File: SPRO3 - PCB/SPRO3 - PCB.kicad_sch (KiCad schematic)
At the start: 14 parts

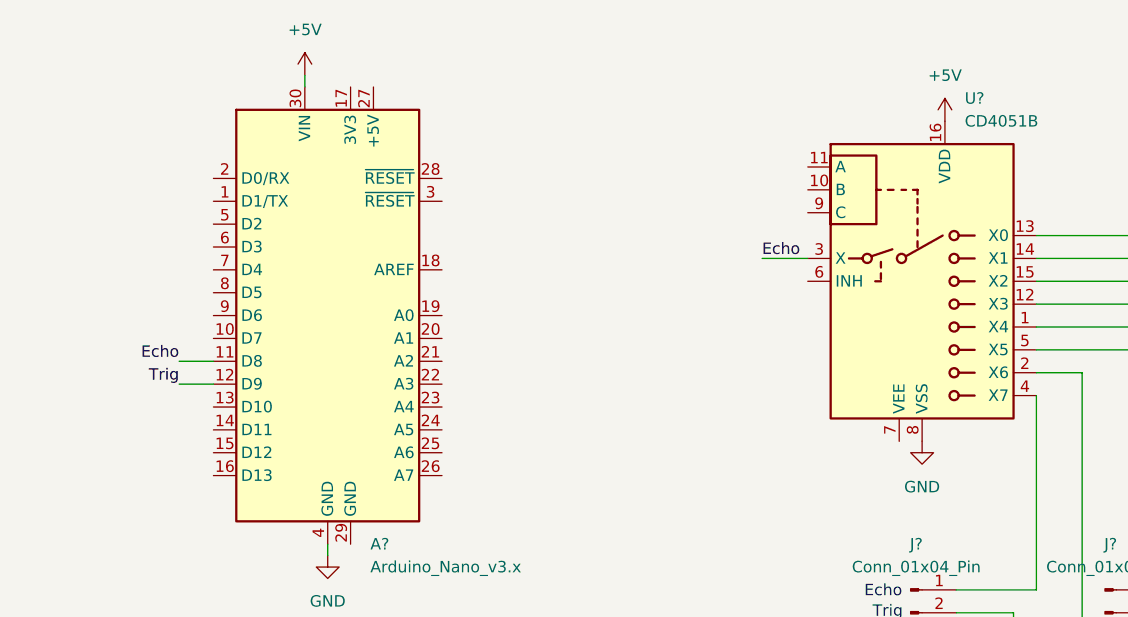
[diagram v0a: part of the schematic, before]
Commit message: Added bypass capacitor to MUX
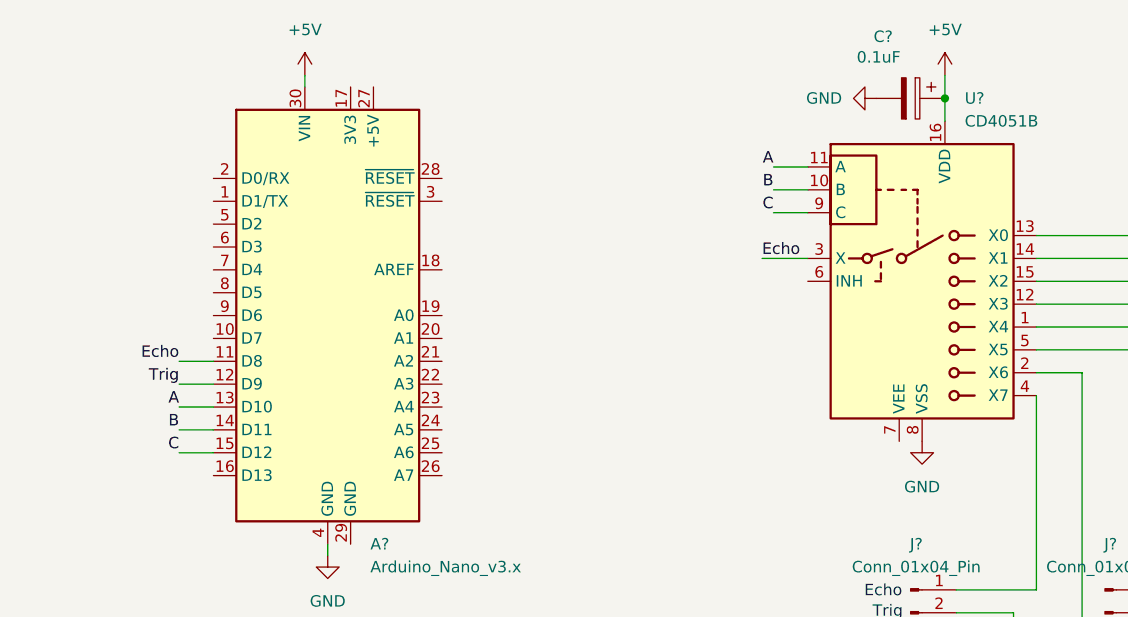
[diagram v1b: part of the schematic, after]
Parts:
- added C?: 0.1uF, symbol Device:C_Polarized
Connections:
- net +5V: now also C?.1
- net GND: now also C?.2
- net A: now reaches A?.13 (D10)
- net A: now also U?.11 (A)
- net B: now reaches A?.14 (D11)
- net B: now also U?.10 (B)
- net C: now reaches A?.15 (D12)
- net C: now also U?.9 (C)

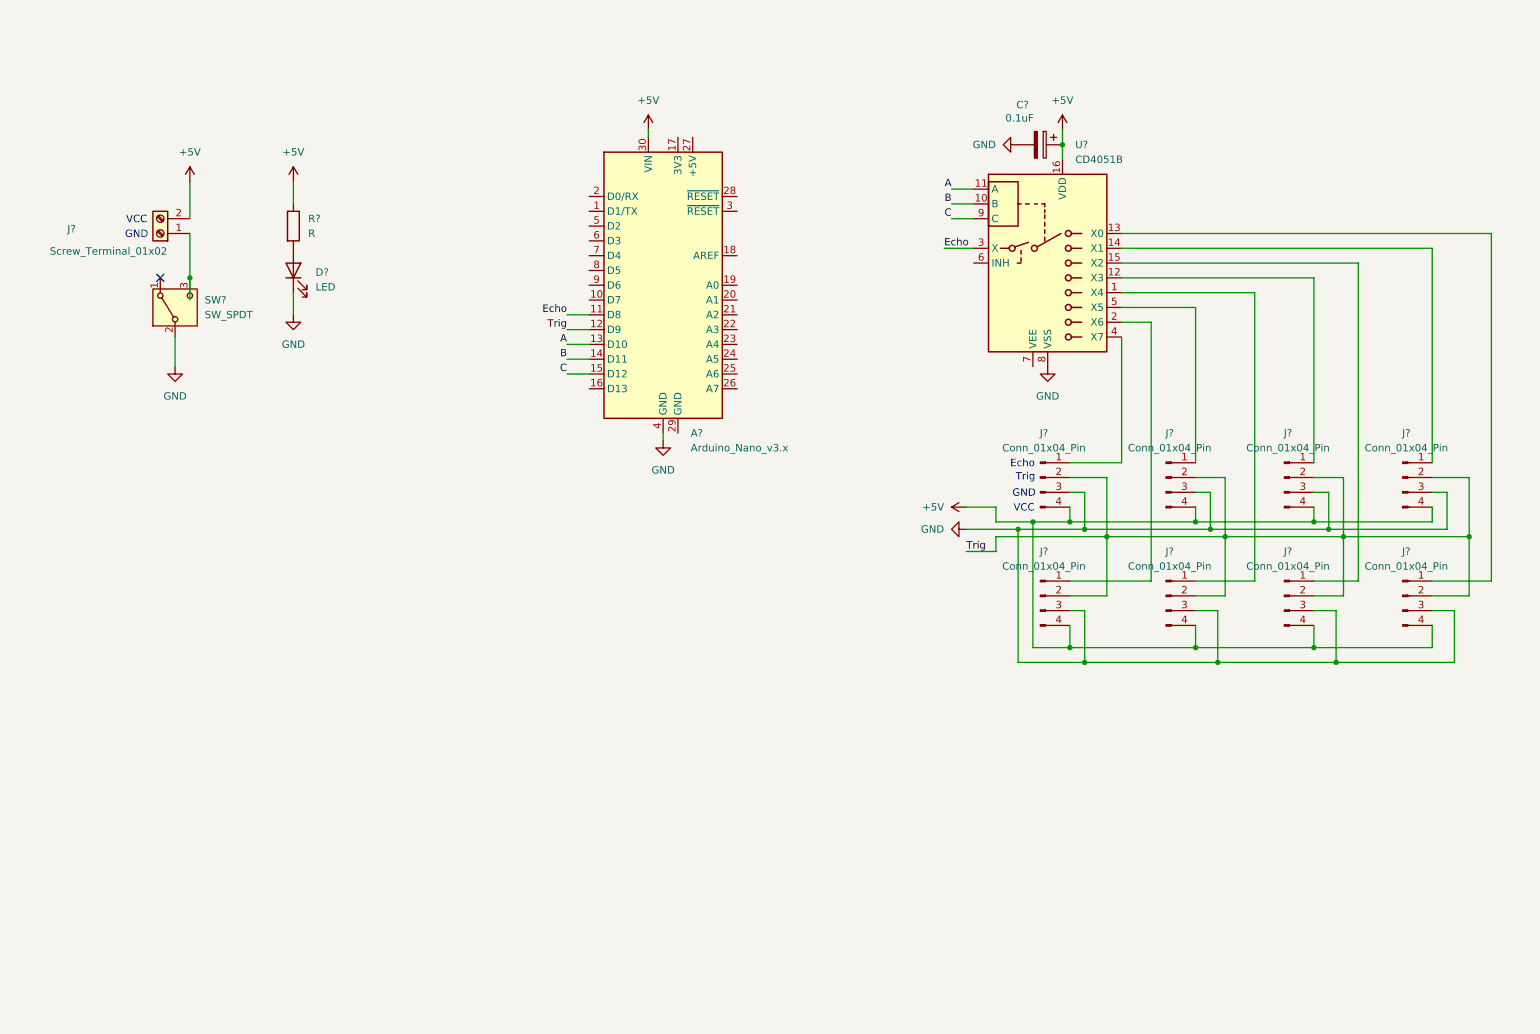
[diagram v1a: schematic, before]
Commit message: udated MUX schematic
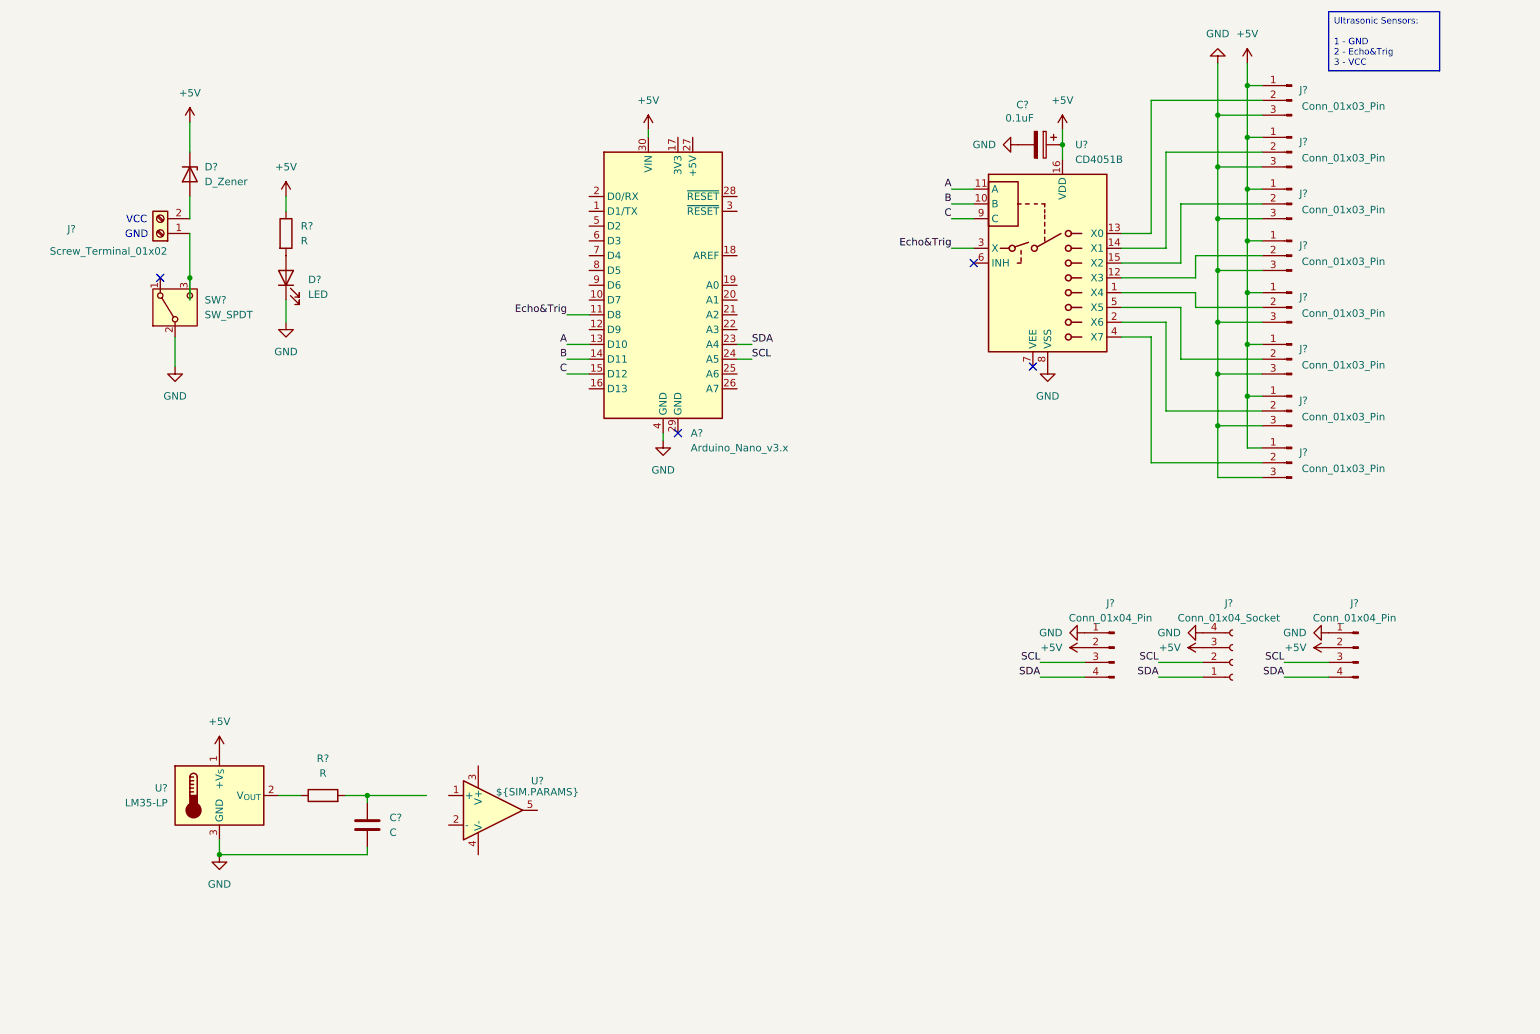
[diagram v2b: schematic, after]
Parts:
- removed J? (x8): Conn_01x04_Pin, symbol Connector:Conn_01x04_Pin
- added C?: C, symbol Device:C
- added D?: D_Zener, symbol Device:D_Zener
- added J? (x8): Conn_01x03_Pin, symbol Connector:Conn_01x03_Pin
- added J?: Conn_01x04_Socket, symbol Connector:Conn_01x04_Socket
- added J? (x2): Conn_01x04_Pin, symbol Connector:Conn_01x04_Pin
- added R?: R, symbol Device:R
- added U?: ${SIM.PARAMS}, symbol Simulation_SPICE:OPAMP
- added U?: LM35-LP, Package_TO_SOT_THT:TO-92_Inline, symbol Sensor_Temperature:LM35-LP
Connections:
- net +5V: now also D?.1 (K), J?.1 (Pin_1), J?.1 (Pin_1), J?.1 (Pin_1), J?.1 (Pin_1), J?.1 (Pin_1), J?.1 (Pin_1), J?.1 (Pin_1), J?.1 (Pin_1), J?.2 (Pin_2), J?.2 (Pin_2), J?.3 (Pin_3), U?.1 (+V_{S}); no longer J?.2 (Pin_2)
- net GND: now also C?.2, J?.1 (Pin_1), J?.1 (Pin_1), J?.3 (Pin_3), J?.3 (Pin_3), J?.3 (Pin_3), J?.3 (Pin_3), J?.3 (Pin_3), J?.3 (Pin_3), J?.3 (Pin_3), J?.3 (Pin_3), J?.4 (Pin_4), U?.3 (GND)
- net SDA: now reaches A?.23 (A4)
- net SDA: now also J?.1 (Pin_1), J?.4 (Pin_4), J?.4 (Pin_4)
- net SCL: now reaches A?.24 (A5)
- net SCL: now also J?.2 (Pin_2), J?.3 (Pin_3), J?.3 (Pin_3)
- net at U?.15 (X2): now also J?.2 (Pin_2)
- net at U?.4 (X7): now also J?.2 (Pin_2)
- net at U?.2 (X6): now also J?.2 (Pin_2)
- net at U?.13 (X0): now also J?.2 (Pin_2)
- net at U?.1 (X4): now also J?.2 (Pin_2)
- net at U?.12 (X3): now also J?.2 (Pin_2)
- net at U?.14 (X1): now also J?.2 (Pin_2)
- net at U?.5 (X5): now also J?.2 (Pin_2)
- net Echo renamed Echo&Trig
- net Trig: no longer names the net of A?.12 (D9)
- new net: R?.1, U?.2 (V_{OUT})
- new net: C?.1, R?.2
- new net: D?.2 (A), J?.2 (Pin_2)
- no-connect marks 1 -> 4
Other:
- note removed: "Echo"
- note removed: "Trig"
- moved on the sheet: D?, R?

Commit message: Added Kicad files for the second PCB that we are making
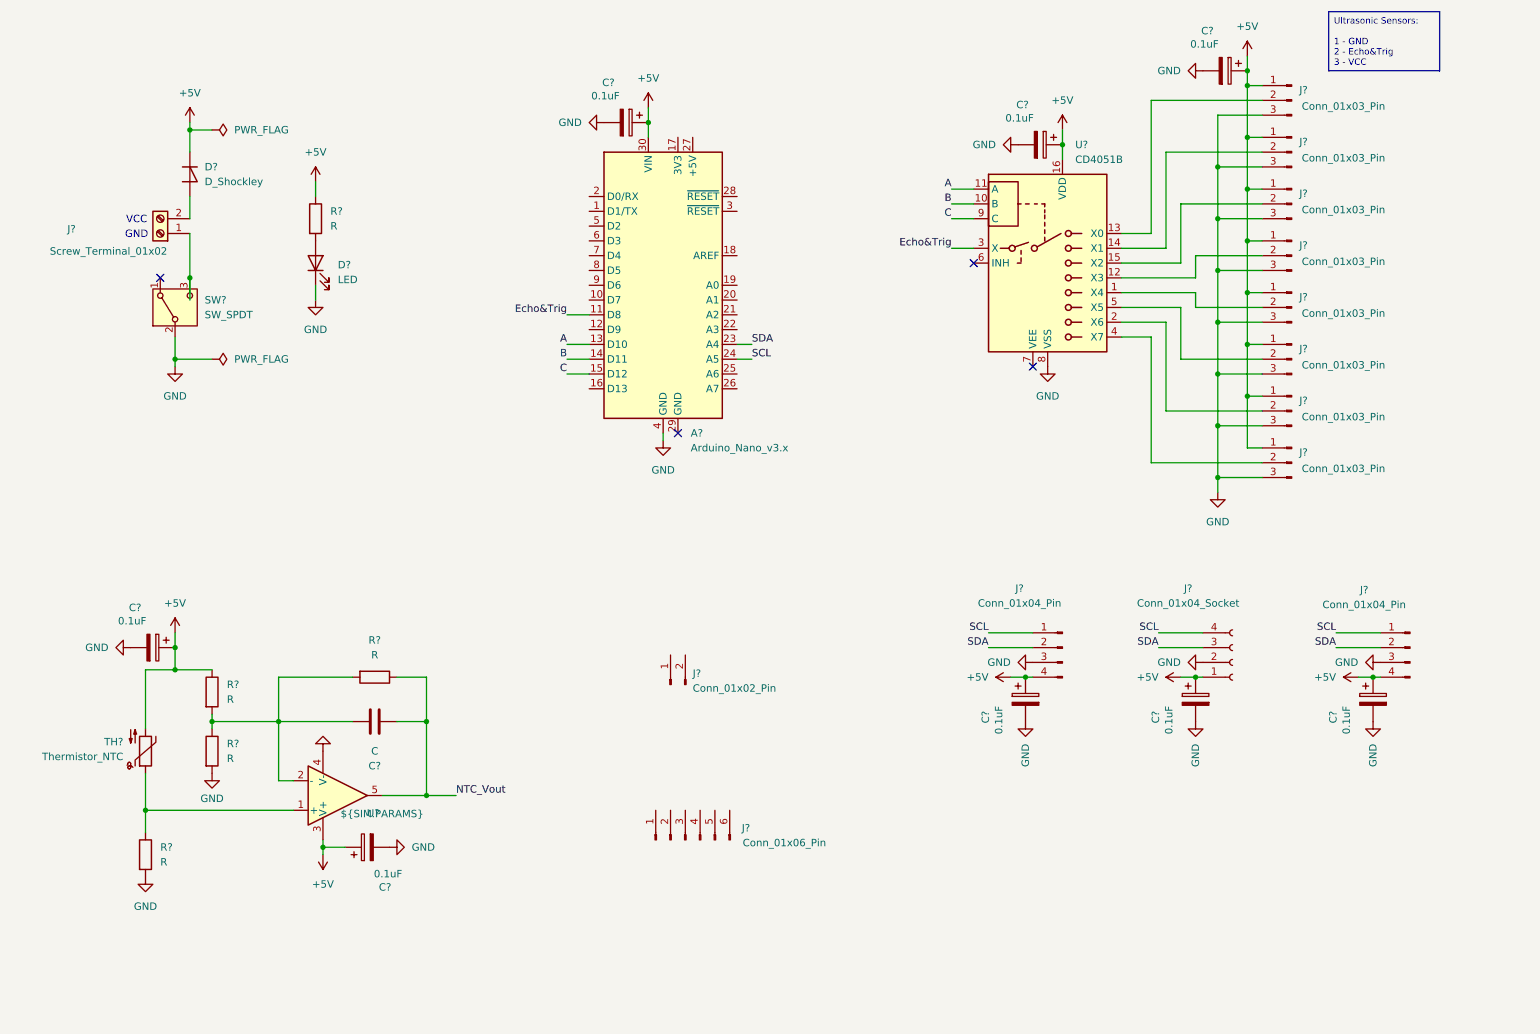
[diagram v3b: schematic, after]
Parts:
- removed C?: C, symbol Device:C
- removed D?: D_Zener, symbol Device:D_Zener
- removed J?: Conn_01x04_Pin, symbol Connector:Conn_01x04_Pin
- removed R?: R, symbol Device:R
- removed U?: LM35-LP, Package_TO_SOT_THT:TO-92_Inline, symbol Sensor_Temperature:LM35-LP
- added C? (x7): 0.1uF, symbol Device:C_Polarized
- added C?: C, symbol Device:C
- added D?: D_Shockley, symbol Device:D_Shockley
- added J?: Conn_01x04_Pin, symbol Connector:Conn_01x04_Pin
- added J?: Conn_01x02_Pin, symbol Connector:Conn_01x02_Pin
- added J?: Conn_01x06_Pin, symbol Connector:Conn_01x06_Pin
- added R? (x4): R, symbol Device:R
- added TH?: Thermistor_NTC, symbol Device:Thermistor_NTC
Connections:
- net +5V: now also J?.1 (Pin_1), J?.4 (Pin_4), U?.3 (V+), C?.1, C?.1, C?.1, C?.1, C?.1, C?.1, C?.1, D?.1 (K), J?.4 (Pin_4), R?.1, TH?.2; no longer J?.2 (Pin_2), J?.3 (Pin_3)
- net GND: now also J?.2 (Pin_2), J?.3 (Pin_3), U?.4 (V-), C?.2, C?.2, C?.2, C?.2, C?.2, C?.2, C?.2, J?.3 (Pin_3), R?.2, R?.2; no longer J?.1 (Pin_1), J?.4 (Pin_4)
- net SCL: now also J?.1 (Pin_1), J?.4 (Pin_4), J?.1 (Pin_1); no longer J?.2 (Pin_2), J?.3 (Pin_3)
- net SDA: now also J?.2 (Pin_2), J?.3 (Pin_3), J?.2 (Pin_2); no longer J?.1 (Pin_1), J?.4 (Pin_4)
- net at U?.1 (+): now also R?.1, TH?.1
- net at U?.2 (-): now also C?.1, R?.1, R?.2, R?.2
- net NTC_Vout: now reaches U?.5
- net NTC_Vout: now also C?.2, R?.1
- net at J?.2 (Pin_2): now also D?.2 (A)
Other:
- moved on the sheet: D?, J?, R?, U?

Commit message: Added labels and pin connections to the main PCB
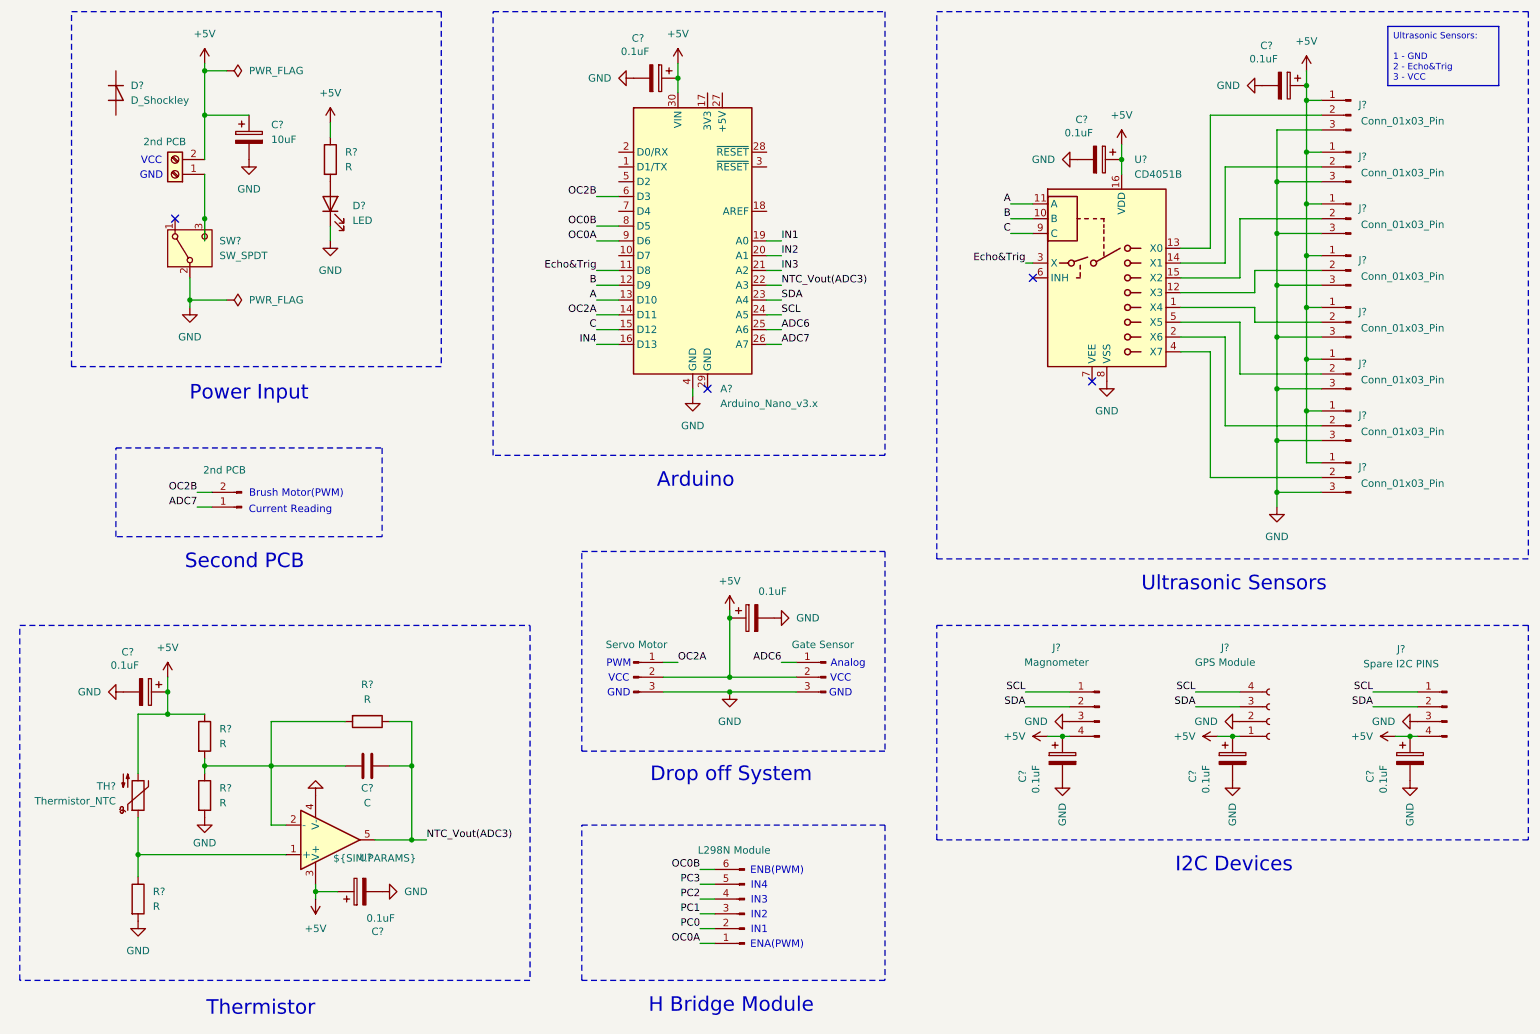
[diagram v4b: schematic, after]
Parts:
- added C?: 0.1uF, symbol Device:C_Polarized
- added C?: 10uF, symbol Device:C_Polarized
- added J?: Gate Sensor, symbol Connector:Conn_01x03_Pin
- added J?: Servo Motor, symbol Connector:Conn_01x03_Pin
- J?: value Conn_01x04_Pin -> Spare I2C PINS
- J?: value Conn_01x04_Socket -> GPS Module
- J?: value Conn_01x02_Pin -> 2nd PCB
- J?: value Conn_01x06_Pin -> L298N Module
- J?: value Conn_01x04_Pin -> Magnometer
- J?: value Screw_Terminal_01x02 -> 2nd PCB
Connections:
- net NTC_Vout is gone; now on net NTC_Vout(ADC3): C?.2, R?.1, U?.5
- net +5V: now also J?.2 (Pin_2), C?.1, C?.1, J?.2 (Pin_2), J?.2 (Pin_2); no longer D?.1 (K)
- net B: now also A?.12 (D9); no longer A?.14 (D11)
- net GND: now also C?.2, C?.2, J?.3 (Pin_3), J?.3 (Pin_3)
- net IN4: now reaches A?.16 (D13)
- net IN1: now reaches A?.19 (A0)
- net IN2: now reaches A?.20 (A1)
- net IN3: now reaches A?.21 (A2)
- net NTC_Vout(ADC3): now reaches A?.22 (A3)
- net ADC6: now reaches A?.25 (A6)
- net ADC6: now also J?.1 (Pin_1)
- net ADC7: now reaches A?.26 (A7)
- net ADC7: now also J?.1 (Pin_1)
- net OC2B: now reaches A?.6 (D3)
- net OC2B: now also J?.2 (Pin_2)
- net OC0B: now reaches A?.8 (D5)
- net OC0B: now also J?.6 (Pin_6)
- net OC0A: now reaches A?.9 (D6)
- net OC0A: now also J?.1 (Pin_1)
- net PC0: now reaches J?.2 (Pin_2)
- net PC1: now reaches J?.3 (Pin_3)
- net PC2: now reaches J?.4 (Pin_4)
- net PC3: now reaches J?.5 (Pin_5)
- net at D?.2 (A): no longer J?.2 (Pin_2)
- new net OC2A: A?.14 (D11), J?.1 (Pin_1)
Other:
- note added: "Analog"
- note added: "Arduino"
- note added: "Brush Motor(PWM)"
- note added: "Current Reading"
- note added: "Drop off System"
- note added: "ENA(PWM)"
- note added: "ENB(PWM)"
- note added: "H Bridge Module"
- note added: "I2C Devices"
- note added: "IN1"
- note added: "IN2"
- note added: "IN3"
- note added: "IN4"
- note added: "PWM"
- note added: "Power Input"
- note added: "Second PCB"
- note added: "Thermistor"
- note added: "Ultrasonic Sensors"
- moved on the sheet: A?, C?, D?, J?, R?, SW?, TH?, U?
